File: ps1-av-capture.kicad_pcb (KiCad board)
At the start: 4 copper layers, 100 x 80 mm, 237 parts, among them J1 AV_PIGTAIL, J2 USB3_B, J3 USB_C_AUDIO, J4 JTAG, J5 UART, SW1 RESET, U1 TVP7002PZP, U10 TLV75733PDBVR, U11 TLV75533PDBVR, U12 PCM2903CDBR, U2 CYUSB3014-BZXI, U3 24LC1025-I/SN, U4 24LC1025-I/SN, U5 TPS563201DDCR, U6 TPS563201DDCR, U7 TPS563201DDCR, U8 TLV75519PDBVR, U9 TLV75519PDBVR, X1 27MHz, Y1 19.2MHz, Y2 12MHz

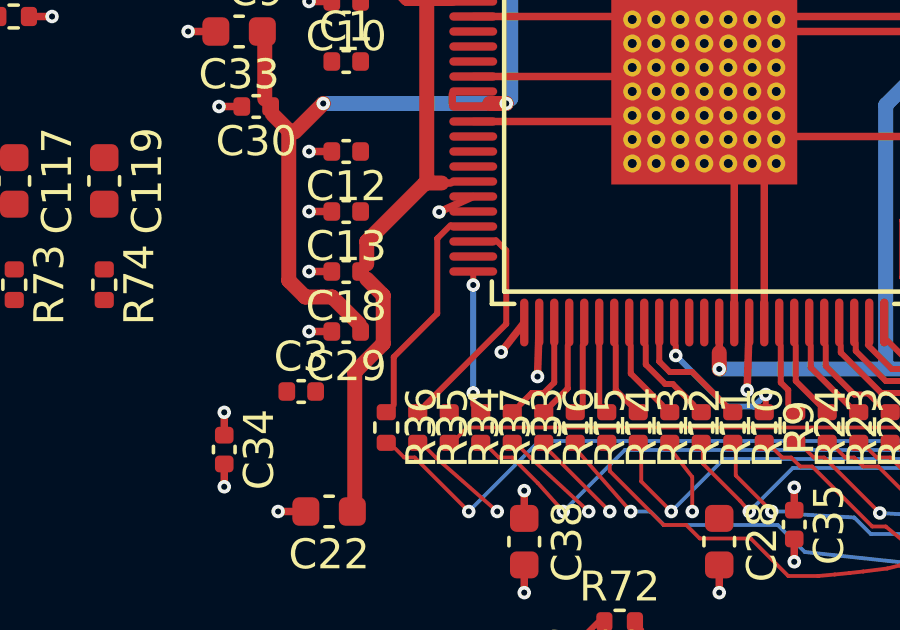
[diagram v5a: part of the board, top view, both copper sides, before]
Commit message: p2p_route: route the four west TVP outs innermost-corner first
TVP_FIDOUT/VSOUT/HSOUT/SOGOUT share one escape south of U1 pins 22-25; the
earlier-routed net walls in the later ones, so TVP_HSOUT's pin was sealed
(no path, 816 expansions) and left unrouted at 1be4c63. Routing SOG, HS, VS,
FID (was FID, VS, HS, SOG) lets each reach its 22R first.
TVP_HSOUT now connected; unconnected 96 -> 95. GPIF 29/29, DRC 0 copper,
In2 breaks >=0.25 mm2 +1V2 1, +3V3 1 (unchanged), no new NECKED/SHORT. Two
builds: identical sorted track lists.
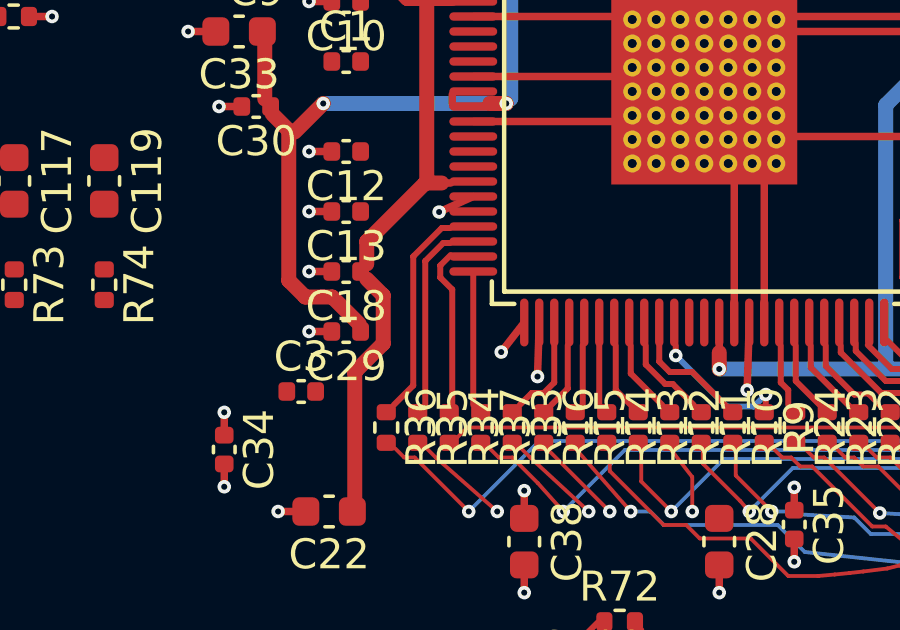
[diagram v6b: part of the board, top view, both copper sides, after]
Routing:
- net TVP_HSOUT: track 0.00 -> 5.31 mm
- net TVP_VSOUT: track 6.76 -> 5.90 mm
- net TVP_SOGOUT: vias 2 -> 0
